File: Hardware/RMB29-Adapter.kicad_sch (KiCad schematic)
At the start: 11 parts, among them J1 CONN IN, J2 CONN OUT, U1 TLV2372

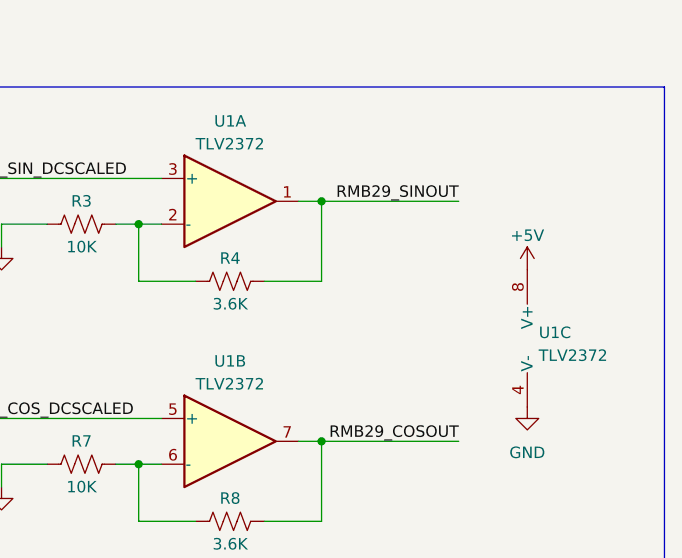
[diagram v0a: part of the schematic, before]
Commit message: Replace TLV272 with MCP602
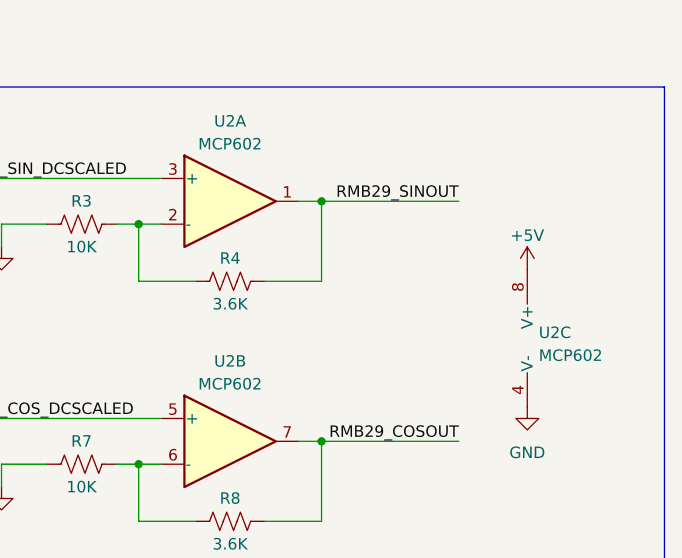
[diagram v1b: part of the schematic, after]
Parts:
- removed U1: TLV2372, symbol Amplifier_Operational:TLV2372
- added U2: MCP602, symbol Amplifier_Operational:MCP602
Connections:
- net +5V: now also U2.8 (V+)
- net GND: now also U2.4 (V-)
- net RMB29_COSOUT: now also U2.7
- net RMB29_COS_DCSCALED: now also U2.5 (+)
- net RMB29_SINOUT: now also U2.1
- net RMB29_SIN_DCSCALED: now also U2.3 (+)
- net at R7.2, R8.1: now also U2.6 (-)
- net at R3.2, R4.1: now also U2.2 (-)
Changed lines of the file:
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@@
+    )
+  )
+  (symbol (lib_id "Amplifier_Operational:MCP602") (at 142.24 62.23 0) (unit 1)
+    (in_bom yes) (on_board yes) (dnp no) (fields_autoplaced)
+    (property "Reference" "U2" (at 142.24 53.34 0)
+      (effects (font (size 1.27 1.27)))
+    )
+    (property "Value" "MCP602" (at 142.24 55.88 0)
+      (effects (font (size 1.27 1.27)))
+    )
+    (property "Footprint" "" (at 142.24 62.23 0)
+      (effects (font (size 1.27 1.27)) hide)
+    )
+    (property "Datasheet" "http://ww1.microchip.com/downloads/en/DeviceDoc/21314g.pdf" (at 142.24 62.23 0)
+      (effects (font (size 1.27 1.27)) hide)
+    )
+    (pin "1")
+    (pin "2")
+    (pin "3")
+    (pin "5")
+    (pin "6")
+    (pin "7")
+    (pin "4")
+    (pin "8")
+    (instances
+      (project "RMB29-Adapter"
+        (path "/22288523-8438-46c9-813f-51eb75fba734"
+          (reference "U2") (unit 1)
+        )
+      )
     )
   )
@@
     )
   )
-  (symbol (lib_id "Amplifier_Operational:TLV2372") (at 142.24 62.23 0) (unit 1)
-    (in_bom yes) (on_board yes) (dnp no) (fields_autoplaced)
-    (property "Reference" "U1" (at 142.24 53.34 0)
-      (effects (font (size 1.27 1.27)))
-    )
-    (property "Value" "TLV2372" (at 142.24 55.88 0)
-      (effects (font (size 1.27 1.27)))
-    )
-    (property "Footprint" "" (at 142.24 62.23 0)
-      (effects (font (size 1.27 1.27)) hide)
-    )
-    (property "Datasheet" "http://www.ti.com/lit/ds/symlink/tlv2375.pdf" (at 142.24 62.23 0)
+  (symbol (lib_id "Device:R_US") (at 104.14 59.69 90) (unit 1)
+    (in_bom yes) (on_board yes) (dnp no) (fields_autoplaced)
+    (property "Reference" "R1" (at 104.14 54.61 90)
+      (effects (font (size 1.27 1.27)))
+    )
+    (property "Value" "10K" (at 104.14 57.15 90)
+      (effects (font (size 1.27 1.27)))
+    )
+    (property "Footprint" "" (at 104.394 58.674 90)
+      (effects (font (size 1.27 1.27)) hide)
+    )
+    (property "Datasheet" "~" (at 104.14 59.69 0)
+      (effects (font (size 1.27 1.27)) hide)
+    )
+    (pin "1")
+    (pin "2")
+    (instances
+      (project "RMB29-Adapter"
+        (path "/22288523-8438-46c9-813f-51eb75fba734"
+          (reference "R1") (unit 1)
+        )
+      )
+    )
+  )
+  (symbol (lib_id "power:GND") (at 116.84 67.31 0) (unit 1)
+    (in_bom yes) (on_board yes) (dnp no)
+    (property "Reference" "#PWR05" (at 116.84 73.66 0)
+      (effects (font (size 1.27 1.27)) hide)
+    )
+    (property "Value" "GND" (at 116.84 71.12 0)
+      (effects (font (size 1.27 1.27)) hide)
+    )
+    (property "Footprint" "" (at 116.84 67.31 0)
+      (effects (font (size 1.27 1.27)) hide)
+    )
+    (property "Datasheet" "" (at 116.84 67.31 0)
+      (effects (font (size 1.27 1.27)) hide)
+    )
+    (pin "1")
+    (instances
+      (project "RMB29-Adapter"
+        (path "/22288523-8438-46c9-813f-51eb75fba734"
+          (reference "#PWR05") (unit 1)
+        )
+      )
+    )
+  )
+  (symbol (lib_id "Amplifier_Operational:MCP602") (at 142.24 88.9 0) (unit 2)
+    (in_bom yes) (on_board yes) (dnp no) (fields_autoplaced)
+    (property "Reference" "U2" (at 142.24 80.01 0)
+      (effects (font (size 1.27 1.27)))
+    )
+    (property "Value" "MCP602" (at 142.24 82.55 0)
+      (effects (font (size 1.27 1.27)))
+    )
+    (property "Footprint" "" (at 142.24 88.9 0)
+      (effects (font (size 1.27 1.27)) hide)
+    )
+    (property "Datasheet" "http://ww1.microchip.com/downloads/en/DeviceDoc/21314g.pdf" (at 142.24 88.9 0)
       (effects (font (size 1.27 1.27)) hide)
     )
@@
       (project "RMB29-Adapter"
         (path "/22288523-8438-46c9-813f-51eb75fba734"
-          (reference "U1") (unit 1)
-        )
-      )
-    )
-  )
-  (symbol (lib_id "Device:R_US") (at 104.14 59.69 90) (unit 1)
-    (in_bom yes) (on_board yes) (dnp no) (fields_autoplaced)
-    (property "Reference" "R1" (at 104.14 54.61 90)
-      (effects (font (size 1.27 1.27)))
-    )
-    (property "Value" "10K" (at 104.14 57.15 90)
-      (effects (font (size 1.27 1.27)))
-    )
-    (property "Footprint" "" (at 104.394 58.674 90)
-      (effects (font (size 1.27 1.27)) hide)
-    )
-    (property "Datasheet" "~" (at 104.14 59.69 0)
-      (effects (font (size 1.27 1.27)) hide)
-    )
-    (pin "1")
-    (pin "2")
-    (instances
-      (project "RMB29-Adapter"
-        (path "/22288523-8438-46c9-813f-51eb75fba734"
-          (reference "R1") (unit 1)
-        )
-      )
-    )
-  )
-  (symbol (lib_id "power:GND") (at 116.84 67.31 0) (unit 1)
-    (in_bom yes) (on_board yes) (dnp no)
-    (property "Reference" "#PWR05" (at 116.84 73.66 0)
-      (effects (font (size 1.27 1.27)) hide)
-    )
-    (property "Value" "GND" (at 116.84 71.12 0)
-      (effects (font (size 1.27 1.27)) hide)
-    )
-    (property "Footprint" "" (at 116.84 67.31 0)
-      (effects (font (size 1.27 1.27)) hide)
-    )
-    (property "Datasheet" "" (at 116.84 67.31 0)
-      (effects (font (size 1.27 1.27)) hide)
-    )
-    (pin "1")
-    (instances
-      (project "RMB29-Adapter"
-        (path "/22288523-8438-46c9-813f-51eb75fba734"
-          (reference "#PWR05") (unit 1)
+          (reference "U2") (unit 2)
         )
       )
@@
     )
   )
-  (symbol (lib_id "Amplifier_Operational:TLV2372") (at 177.8 77.47 0) (unit 3)
-    (in_bom yes) (on_board yes) (dnp no) (fields_autoplaced)
-    (property "Reference" "U1" (at 176.53 76.835 0)
+  (symbol (lib_id "Amplifier_Operational:MCP602") (at 177.8 77.47 0) (unit 3)
+    (in_bom yes) (on_board yes) (dnp no) (fields_autoplaced)
+    (property "Reference" "U2" (at 176.53 76.835 0)
       (effects (font (size 1.27 1.27)) (justify left))
     )
-    (property "Value" "TLV2372" (at 176.53 79.375 0)
+    (property "Value" "MCP602" (at 176.53 79.375 0)
       (effects (font (size 1.27 1.27)) (justify left))
     )
@@
       (effects (font (size 1.27 1.27)) hide)
     )
-    (property "Datasheet" "http://www.ti.com/lit/ds/symlink/tlv2375.pdf" (at 177.8 77.47 0)
+    (property "Datasheet" "http://ww1.microchip.com/downloads/en/DeviceDoc/21314g.pdf" (at 177.8 77.47 0)
       (effects (font (size 1.27 1.27)) hide)
     )
@@
       (project "RMB29-Adapter"
         (path "/22288523-8438-46c9-813f-51eb75fba734"
-          (reference "U1") (unit 3)
+          (reference "U2") (unit 3)
         )
       )
@@
         )
       )
-    )
-  )
-  (symbol (lib_id "Amplifier_Operational:TLV2372") (at 142.24 88.9 0) (unit 2)
-    (in_bom yes) (on_board yes) (dnp no) (fields_autoplaced)
-    (property "Reference" "U1" (at 142.24 80.01 0)
-      (effects (font (size 1.27 1.27)))
-    )
-    (property "Value" "TLV2372" (at 142.24 82.55 0)
-      (effects (font (size 1.27 1.27)))
-    )
-    (property "Footprint" "" (at 142.24 88.9 0)
-      (effects (font (size 1.27 1.27)) hide)
-    )
-    (property "Datasheet" "http://www.ti.com/lit/ds/symlink/tlv2375.pdf" (at 142.24 88.9 0)
-      (effects (font (size 1.27 1.27)) hide)
-    )
-    (pin "1")
-    (pin "2")
-    (pin "3")
-    (pin "5")
-    (pin "6")
-    (pin "7")
-    (pin "4")
-    (pin "8")
-    (instances
-      (project "RMB29-Adapter"
-        (path "/22288523-8438-46c9-813f-51eb75fba734"
-          (reference "U1") (unit 2)
-        )
-      )

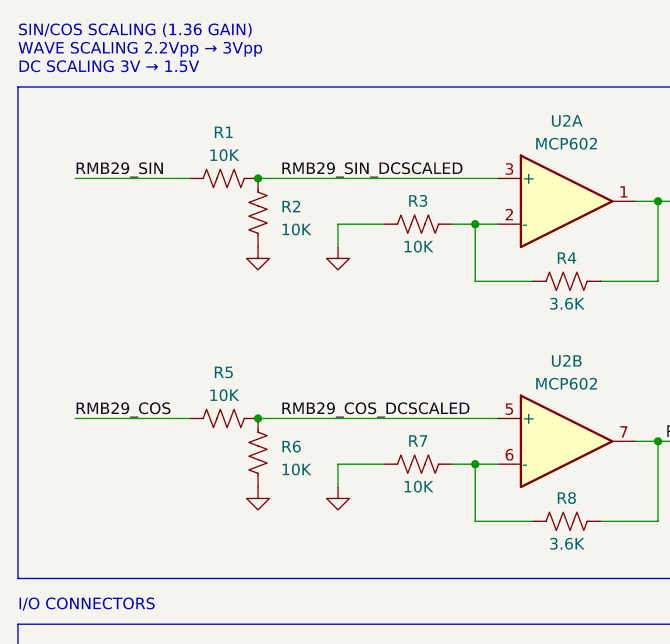
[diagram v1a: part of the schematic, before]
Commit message: Fix offset gain resistors
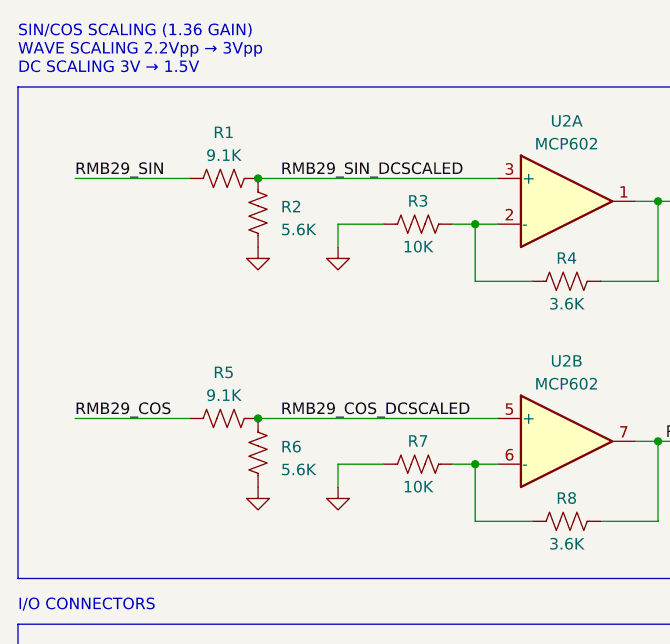
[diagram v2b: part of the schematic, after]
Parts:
- R1, R5: value 10K -> 9.1K
- R2, R6: value 10K -> 5.6K
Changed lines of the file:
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@@
       (effects (font (size 1.27 1.27)) (justify left))
     )
-    (property "Value" "10K" (at 110.49 65.405 0)
+    (property "Value" "5.6K" (at 110.49 65.405 0)
       (effects (font (size 1.27 1.27)) (justify left))
     )
@@
       (effects (font (size 1.27 1.27)))
     )
-    (property "Value" "10K" (at 104.14 83.82 90)
+    (property "Value" "9.1K" (at 104.14 83.82 90)
       (effects (font (size 1.27 1.27)))
     )
@@
       (effects (font (size 1.27 1.27)) (justify left))
     )
-    (property "Value" "10K" (at 110.49 92.075 0)
+    (property "Value" "5.6K" (at 110.49 92.075 0)
       (effects (font (size 1.27 1.27)) (justify left))
     )
@@
       (effects (font (size 1.27 1.27)))
     )
-    (property "Value" "10K" (at 104.14 57.15 90)
-      (effects (font (size 1.27 1.27)))
-    )
+    (property "Value" "9.1K" (at 104.14 57.15 90)
+      (effects (font (size 1.27 1.27)))
+    )

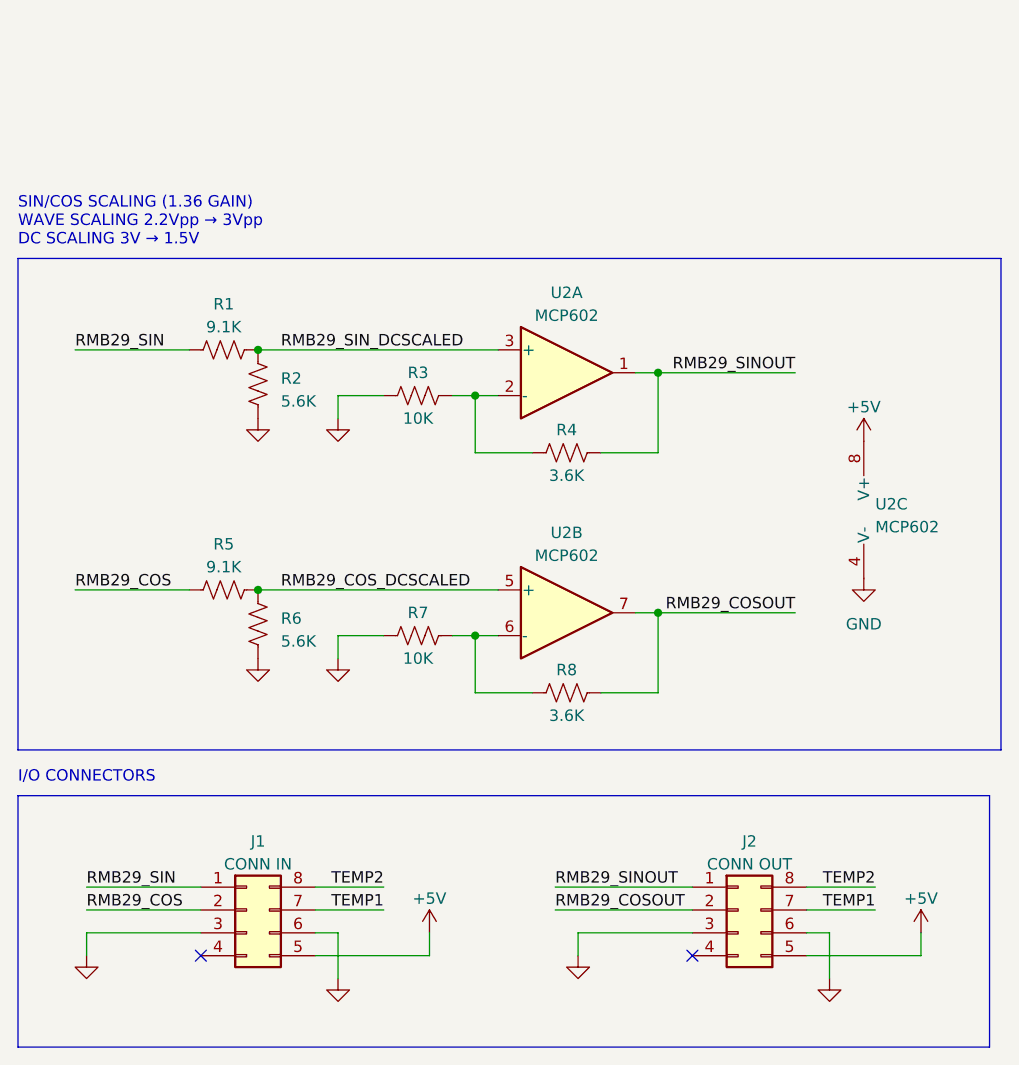
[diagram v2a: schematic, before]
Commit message: New motor encoder
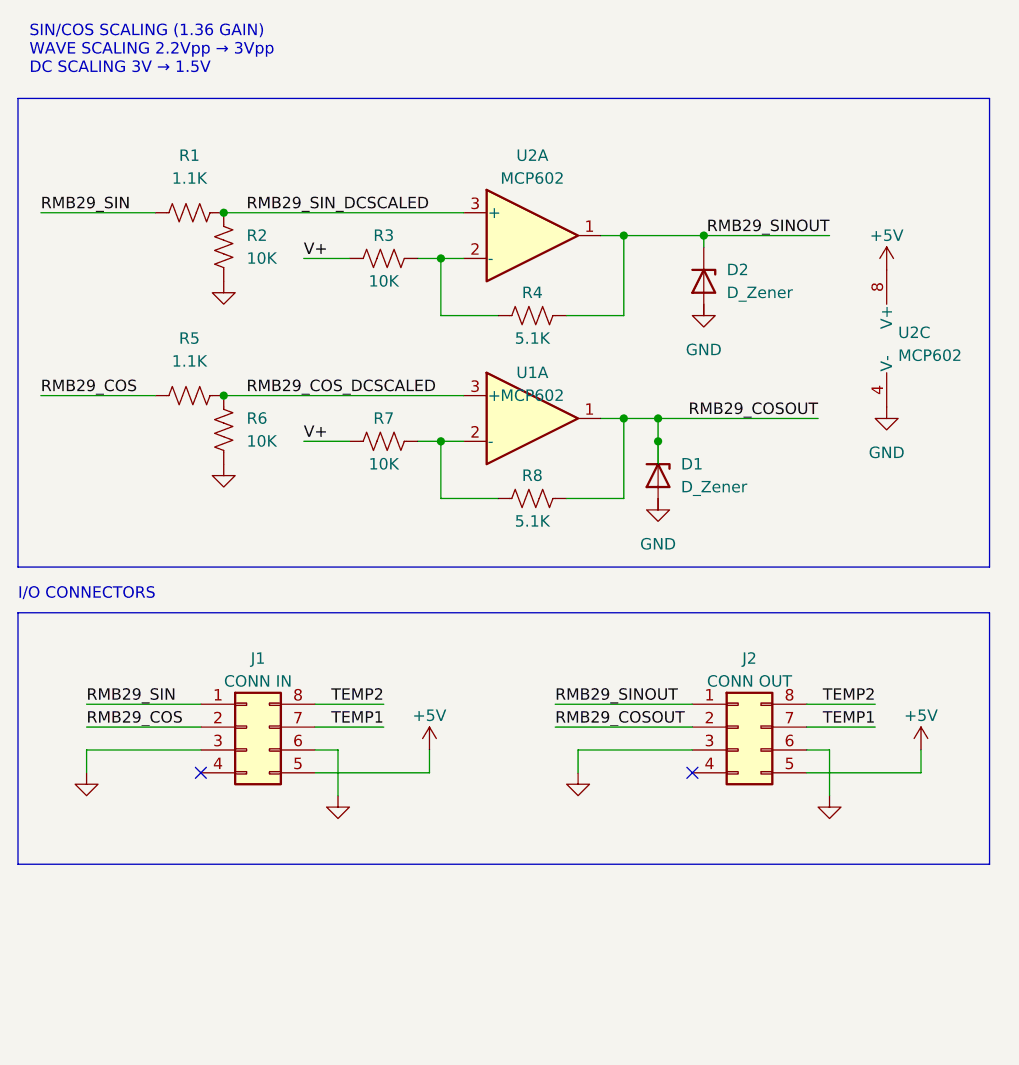
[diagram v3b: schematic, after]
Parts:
- removed unit 2 of U2
- added D1, D2: D_Zener, MMSZener (3.3V):SOD123_DIO, symbol Device:D_Zener
- added U1: MCP602, MCP6002:PDIP8_300MC_MCH, symbol Amplifier_Operational:MCP602
- J1: footprint (none) -> Connector_Molex:Molex_Mini-Fit_Jr_5566-08A_2x04_P4.20mm_Vertical
- J2: footprint (none) -> Connector_JST:JST_PH_B8B-PH-K_1x08_P2.00mm_Vertical
- R1, R5: value 9.1K -> 1.1K; footprint (none) -> Resistor_SMD:R_0805_2012Metric_Pad1.20x1.40mm_HandSolder
- R2, R6: value 5.6K -> 10K; footprint (none) -> Resistor_SMD:R_0805_2012Metric_Pad1.20x1.40mm_HandSolder
- R3, R7: footprint (none) -> Resistor_SMD:R_0805_2012Metric_Pad1.20x1.40mm_HandSolder
- R4, R8: value 3.6K -> 5.1K; footprint (none) -> Resistor_SMD:R_0805_2012Metric_Pad1.20x1.40mm_HandSolder
- U2: footprint (none) -> MCP6002:PDIP8_300MC_MCH
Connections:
- net GND: no longer R3.1, R7.1
- net RMB29_COSOUT: now also D1.1 (K), U1.1
- net RMB29_COS_DCSCALED: now also U1.3 (+)
- net RMB29_SINOUT: now also D2.1 (K)
- net at R7.2, R8.1: now also U1.2 (-)
- new net V+: R3.1, R7.1
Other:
- moved on the sheet: R1, R2, R3, R4, U2A, U2C
